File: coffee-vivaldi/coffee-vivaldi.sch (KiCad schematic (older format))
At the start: 74 parts, among them J1 Conn_Coaxial, J2 AudioPlug3, SW1 SW_SPDT, U1 Opamp_Quad_Generic, U3 OPA1604

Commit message: Added chosen RF components to library and schematic
VCO, PA, and the mixer.
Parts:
- removed C?: 1000p, symbol Device:C
- removed C? (x2): 1.5p, symbol Device:C
- removed C? (x5): 0.1u, symbol Device:C
- removed C? (x3): 47p, symbol Device:C
- removed C?: 10u, symbol Device:C
- removed L?: 10n, symbol Device:L
- removed R?: 10, symbol Device:R
- removed R?: 619, symbol Device:R
- removed R?: 100k, symbol Device:R
- removed R?: T2, symbol Device:R
- removed R?: T1, symbol Device:R
- removed U?: MAAPSS0075, symbol HS2_Parts:MAAPSS0075
- added C?: 0.1uF, symbol Device:C
- added C? (x2): 220pF, symbol Device:C
- added C? (x4): 100uF, symbol Device:C
- added C?: CP, symbol Device:CP
- added L?: L, symbol Device:L
- added R? (x4): 7.15K, symbol Device:R
- added U?: MAX2750AUA+, symbol coffee-vivaldi-rescue:MAX2750AUA+-coffee-vivaldi-cache
- added U?: SE2565T-R, symbol coffee-vivaldi-rescue:SE2565T-R-coffee-vivaldi-cache
- added U?: MAX2681EUT+T, symbol coffee-vivaldi-rescue:MAX2681EUT+T-coffee-vivaldi-cache
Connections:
- net labels added: IF_OUTPUT, INPUT_FROM_SYNTHESIZER, NEEDS_TO_BE_HIGH_TO_TURN_ON_DEVICE, RF_INPUT_MIXER, SHUTDOWN_CONTROL1, TO_ATTENUATOR, TO_VCC, VCC_MIXER
- net labels removed: RFIN, RFOUT, VCC, Ven, Vm
- wire segments 180 -> 196
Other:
- note added: "MIXER"
- note added: "PA"
- note added: "VCO"
- moved on the sheet: BT1, BT2, C1, C10, C11, C12, C13, C2, C3, C4, C5, C6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

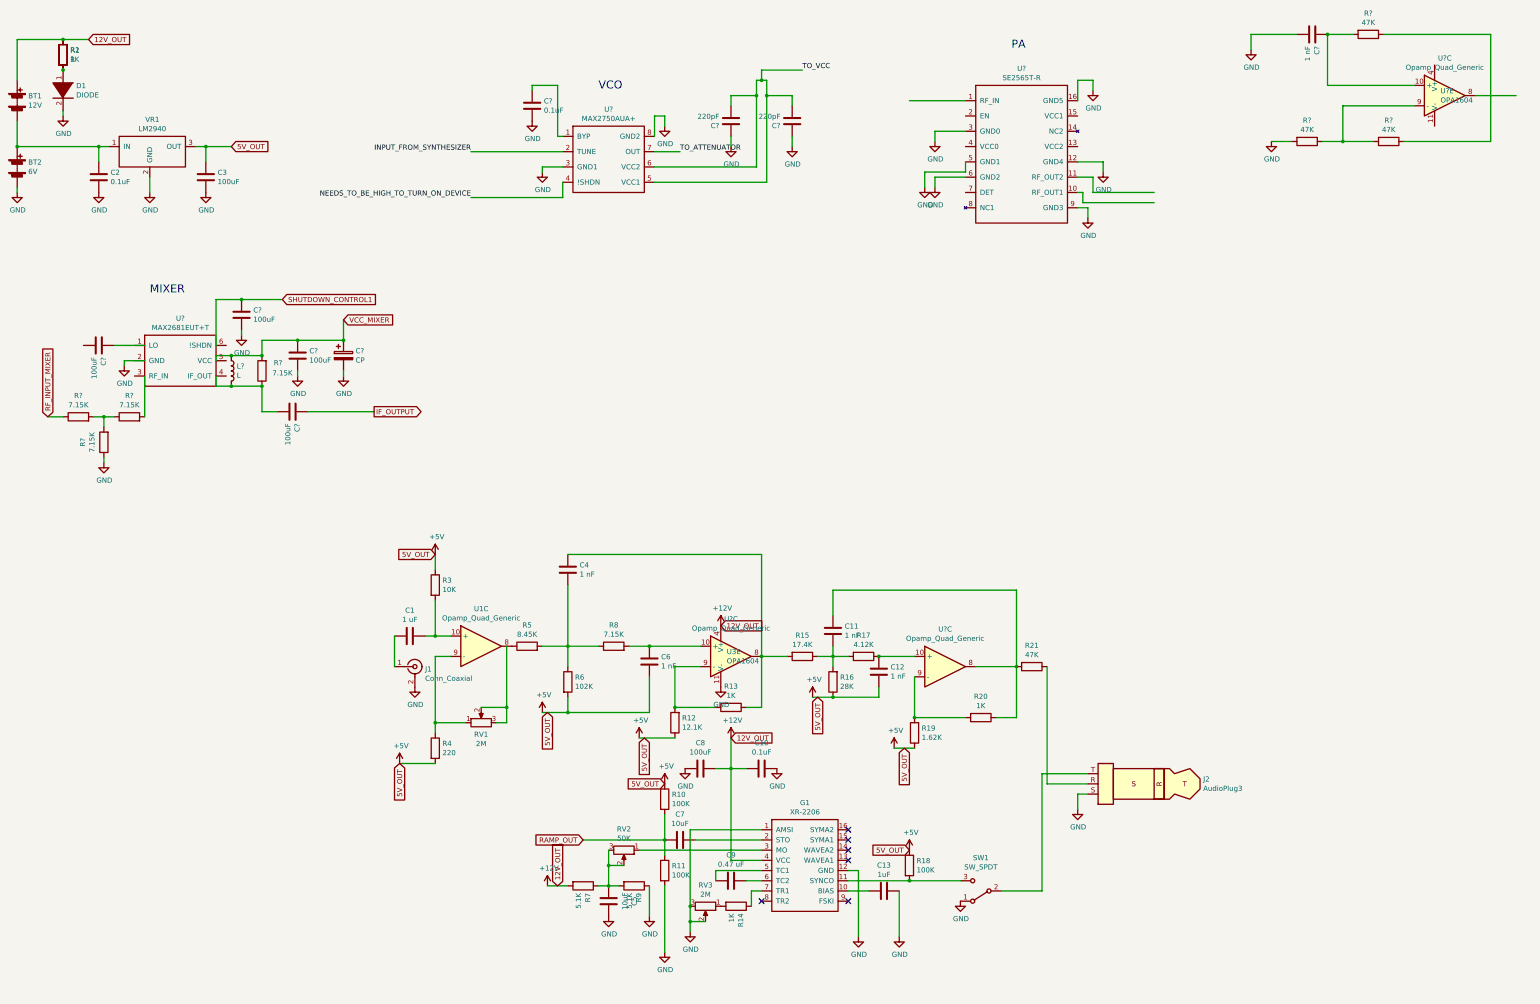
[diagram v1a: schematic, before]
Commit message: Adding passive elements with the RF chips
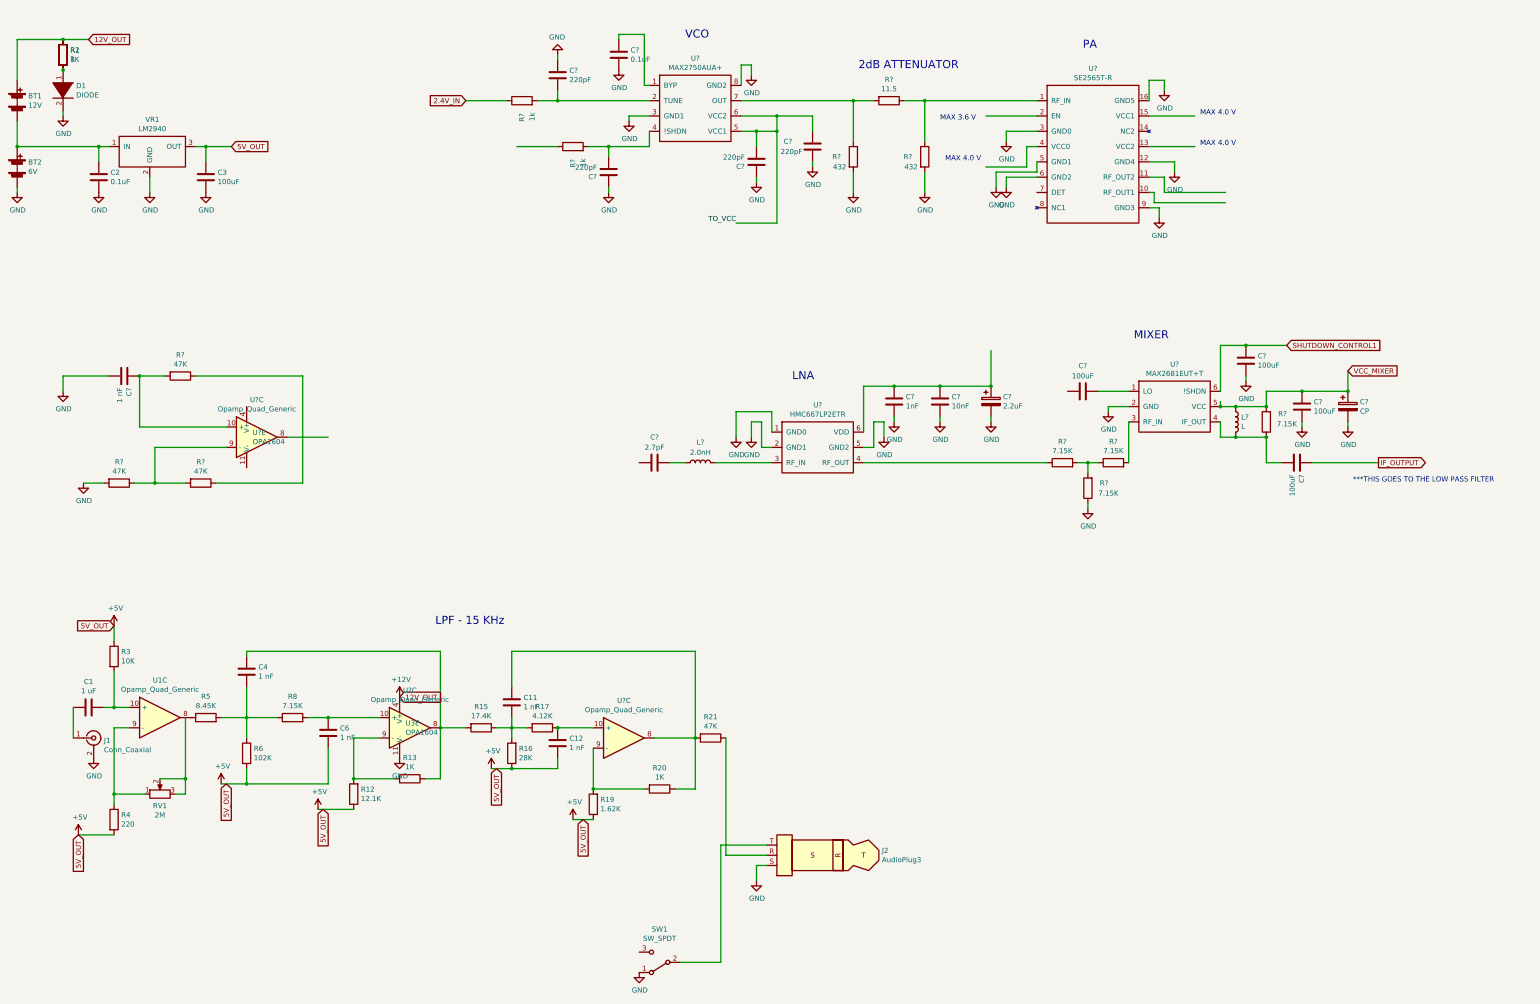
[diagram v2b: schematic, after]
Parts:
- removed C10: 0.1uF, symbol Device:C
- removed C13: 1uF, symbol Device:C
- removed C5, C7: 10uF, symbol Device:C
- removed C8: 100uF, symbol Device:C
- removed C9: 0.47 uF, symbol Device:C
- removed G1: XR-2206, symbol HS2_Parts:XR-2206
- removed R10, R11, R18: 100K, symbol Device:R
- removed R14: 1K, symbol Device:R
- removed R7, R9: 5.1K, symbol Device:R
- removed RV2: 50K, symbol Device:R_POT
- removed RV3: 2M, symbol Device:R_POT
- removed U?: MAX2681EUT+T, symbol coffee-vivaldi-rescue:MAX2681EUT+T-coffee-vivaldi-cache
- added C?: 2.7pF, symbol Device:C
- added C?: 1nF, symbol Device:C
- added C?: 2.2uF, symbol Device:CP
- added C?: 10nF, symbol Device:C
- added C? (x2): 220pF, symbol Device:C
- added L?: 2.0nH, symbol Device:L
- added R? (x2): 1k, symbol Device:R
- added R?: 11.5, symbol Device:R
- added R? (x2): 432, symbol Device:R
- added U?: HMC667LP2ETR, symbol coffee-vivaldi-rescue:HMC667LP2ETR-coffee-vivaldi-cache
- added U?: MAX2681EUT+T, symbol coffee-vivaldi-rescue:MAX2681EUT+T-coffee-vivaldi-cache
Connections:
- net labels added: 2.4V_IN
- net labels removed: INPUT_FROM_SYNTHESIZER, NEEDS_TO_BE_HIGH_TO_TURN_ON_DEVICE, RAMP_OUT, RF_INPUT_MIXER, TO_ATTENUATOR
- wire segments 196 -> 199
- no-connect marks 6 -> 0
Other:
- note added: "***THIS GOES TO THE LOW PASS FILTER"
- note added: "2dB ATTENUATOR"
- note added: "LNA"
- note added: "LPF - 15 KHz"
- note added: "MAX 3.6 V"
- note added: "MAX 4.0 V"
- moved on the sheet: C1, C11, C12, C4, C6, C?, J1, J2, L?, R12, R13, R15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

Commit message: Edited radar schematic
Still a work in progress.
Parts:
- removed J1: Conn_Coaxial, symbol Connector:Conn_Coaxial
- removed R? (x4): 7.15K, symbol Device:R
- removed U?: HMC667LP2ETR, symbol coffee-vivaldi-rescue:HMC667LP2ETR-coffee-vivaldi-cache
- removed U?: Opamp_Quad_Generic, symbol Device:Opamp_Quad_Generic
- removed U?: MAX2681EUT+T, symbol coffee-vivaldi-rescue:MAX2681EUT+T-coffee-vivaldi-cache
- removed U?: MAX2750AUA+, symbol coffee-vivaldi-rescue:MAX2750AUA+-coffee-vivaldi-cache
- removed U?: SE2565T-R, symbol coffee-vivaldi-rescue:SE2565T-R-coffee-vivaldi-cache
- added C10: 0.1uF, symbol Device:C
- added C13: 1uF, symbol Device:C
- added C5, C7: 10uF, symbol Device:C
- added C8: 100uF, symbol Device:C
- added C9: 0.47 uF, symbol Device:C
- added C?: 270pF, symbol Device:C
- added G1: XR-2206, symbol HS2_Parts:XR-2206
- added L?: 1.2nH, symbol Device:L
- added R10, R11, R18: 100K, symbol Device:R
- added R14: 1K, symbol Device:R
- added R7, R9: 5.1K, symbol Device:R
- added RV2: 50K, symbol Device:R_POT
- added RV3: 2M, symbol Device:R_POT
- added U?: MAX2681EUT+T, symbol HS2_Parts:MAX2681EUT+T
- added U?: HMC667LP2ETR, symbol HS2_Parts:HMC667LP2ETR
- added U?: MAX2750AUA+, symbol HS2_Parts:MAX2750AUA+
- added U?: SE2565T-R, symbol HS2_Parts:SE2565T-R
- added U? (x2): SMA_PCB_Edge_Mount, symbol HS2_Parts:SMA_PCB_Edge_Mount
- added U?: Opamp_Quad_Generic, symbol Device:Opamp_Quad_Generic
- C?: value 100uF -> 3pF
- C?: value CP -> 10uF
- L?: value L -> 82nH
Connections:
- net labels added: 3.6V_IN, 3.6V_OUT, 4.0V_IN, 4.0V_OUT, COUPLER_SIGNAL, IF_SIGNAL, RAMP_SIGNAL
- net labels removed: 2.4V_IN, IF_OUTPUT, SHUTDOWN_CONTROL1, TO_VCC
- wire segments 199 -> 243
- no-connect marks 0 -> 7
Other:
- note added: "MODULATOR"
- note added: "Rx"
- note added: "Tx"
- note removed: "***THIS GOES TO THE LOW PASS FILTER"
- note removed: "MAX 3.6 V"
- note removed: "MAX 4.0 V"
- moved on the sheet: C1, C6, C?, L?, R21, R3, R4, R6, R8, R?, SW1, U1C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

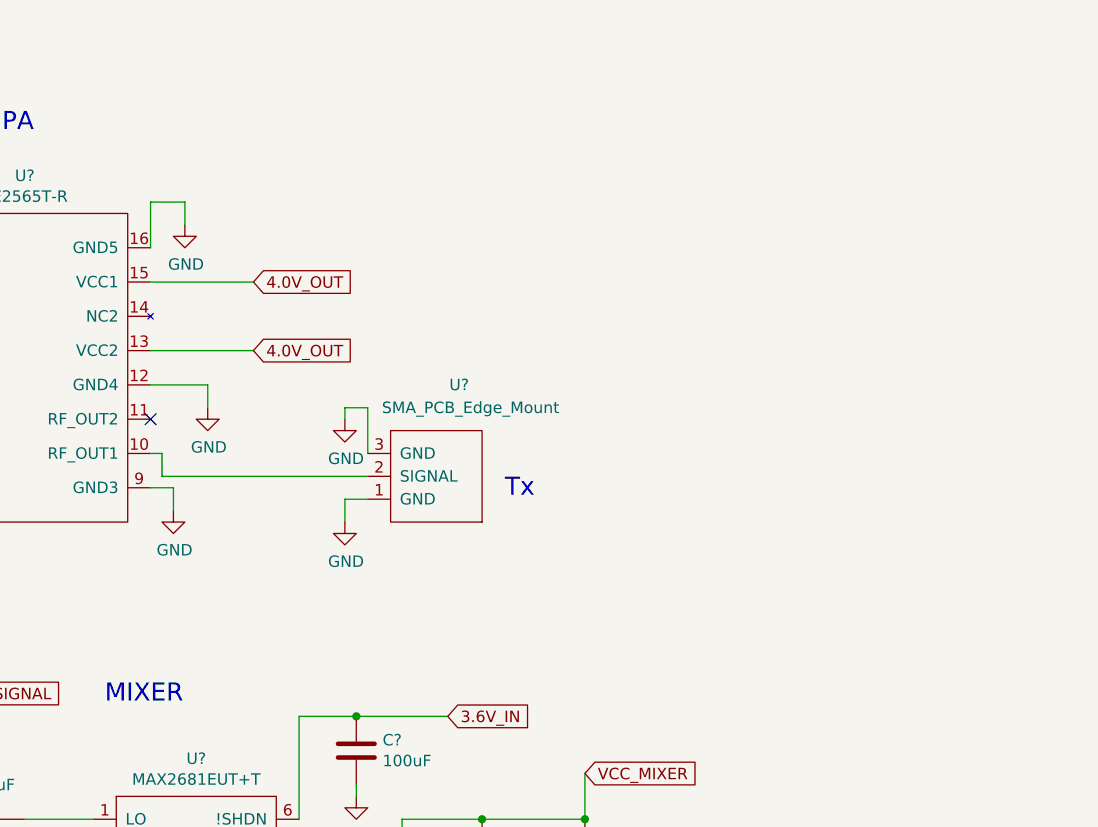
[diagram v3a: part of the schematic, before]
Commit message: Added directional coupler, added impedence control
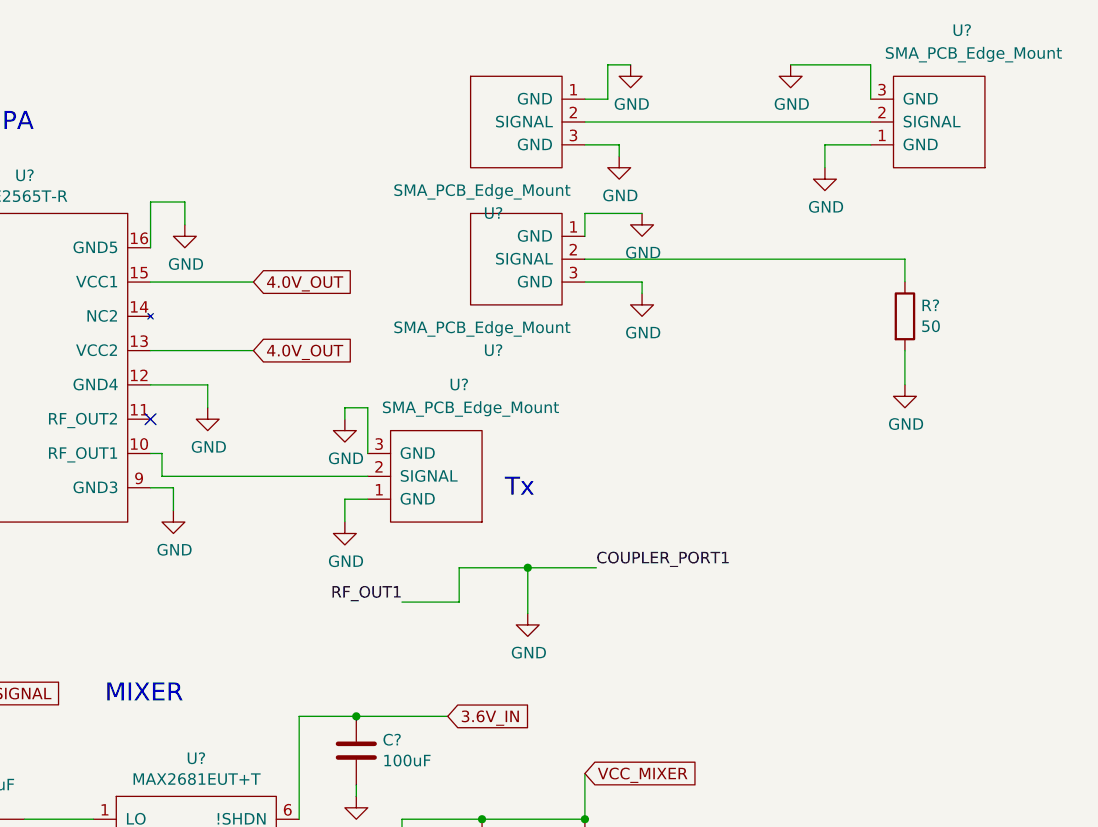
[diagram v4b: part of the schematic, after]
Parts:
- added R?: 50, symbol Device:R
- added U? (x3): SMA_PCB_Edge_Mount, symbol HS2_Parts:SMA_PCB_Edge_Mount
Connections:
- net GND: now also R?.2, U?.1 (GND), U?.1 (GND), U?.1 (GND), U?.3 (GND), U?.3 (GND), U?.3 (GND)
- new net: U?.2 (SIGNAL), U?.2 (SIGNAL)
- new net: R?.1, U?.2 (SIGNAL)
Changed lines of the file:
@@
 Text GLabel 5900 2300 0    50   Input ~ 0
 3.6V_OUT
-Wire Wire Line
-	13050 2850 12150 2850
 Text Notes 13650 2950 0    79   ~ 0
 Tx
@@
 Text GLabel 8050 3050 0    50   Input ~ 0
 5V_OUT
+$Comp
+L HS2_Parts:SMA_PCB_Edge_Mount U?
+U 1 1 60438739
+P 13700 1500
+F 0 "U?" H 13600 1300 50  0000 C CNN
+F 1 "SMA_PCB_Edge_Mount" H 13550 1400 50  0000 C CNN
+F 2 "" H 13700 1500 50  0001 C CNN
+F 3 "" H 13700 1500 50  0001 C CNN
+	1    13700 1500
+	1    0    0    -1
+$EndComp
+$Comp
+L HS2_Parts:SMA_PCB_Edge_Mount U?
+U 1 1 6043955D
+P 15550 1100
+F 0 "U?" H 15450 900 50  0000 C CNN
+F 1 "SMA_PCB_Edge_Mount" H 15400 1000 50  0000 C CNN
+F 2 "" H 15550 1100 50  0001 C CNN
+F 3 "" H 15550 1100 50  0001 C CNN
+	1    15550 1100
+	-1   0    0    1
+$EndComp
+Wire Wire Line
+	12150 2850 13050 2850
+Wire Wire Line
+	13200 3400 13450 3400
+Wire Wire Line
+	13450 3400 13450 3250
+Wire Wire Line
+	13450 3250 13750 3250
+Wire Wire Line
+	14000 1300 15250 1300
+$Comp
+L HS2_Parts:SMA_PCB_Edge_Mount U?
+U 1 1 604AA8E4
+P 13700 2100
+F 0 "U?" H 13600 1900 50  0000 C CNN
+F 1 "SMA_PCB_Edge_Mount" H 13550 2000 50  0000 C CNN
+F 2 "" H 13700 2100 50  0001 C CNN
+F 3 "" H 13700 2100 50  0001 C CNN
+	1    13700 2100
+	1    0    0    -1
+$EndComp
+$Comp
+L power:GND #PWR?
+U 1 1 604BD349
+P 14250 1700
+F 0 "#PWR?" H 14250 1450 50  0001 C CNN
+F 1 "GND" H 14255 1527 50  0000 C CNN
+F 2 "" H 14250 1700 50  0001 C CNN
+F 3 "" H 14250 1700 50  0001 C CNN
+	1    14250 1700
+	1    0    0    -1
+$EndComp
+$Comp
+L power:GND #PWR?
+U 1 1 604BD6D7
+P 14250 2050
+F 0 "#PWR?" H 14250 1800 50  0001 C CNN
+F 1 "GND" H 14255 1877 50  0000 C CNN
+F 2 "" H 14250 2050 50  0001 C CNN
+F 3 "" H 14250 2050 50  0001 C CNN
+	1    14250 2050
+	1    0    0    -1
+$EndComp
+$Comp
+L power:GND #PWR?
+U 1 1 604BDAC7
+P 15400 2450
+F 0 "#PWR?" H 15400 2200 50  0001 C CNN
+F 1 "GND" H 15405 2277 50  0000 C CNN
+F 2 "" H 15400 2450 50  0001 C CNN
+F 3 "" H 15400 2450 50  0001 C CNN
+	1    15400 2450
+	1    0    0    -1
+$EndComp
+Wire Wire Line
+	14250 1700 14000 1700
+Wire Wire Line
+	14000 1700 14000 1800
+Wire Wire Line
+	14000 2000 14250 2000
+Wire Wire Line
+	14250 2000 14250 2050
+$Comp
+L power:GND #PWR?
+U 1 1 605037D3
+P 14150 1450
+F 0 "#PWR?" H 14150 1200 50  0001 C CNN
+F 1 "GND" H 14155 1277 50  0000 C CNN
+F 2 "" H 14150 1450 50  0001 C CNN
+F 3 "" H 14150 1450 50  0001 C CNN
+	1    14150 1450
+	1    0    0    -1
+$EndComp
+Wire Wire Line
+	14000 1400 14150 1400
+Wire Wire Line
+	14150 1400 14150 1450
+$Comp
+L power:GND #PWR?
+U 1 1 6051563D
+P 14200 1050
+F 0 "#PWR?" H 14200 800 50  0001 C CNN
+F 1 "GND" H 14205 877 50  0000 C CNN
+F 2 "" H 14200 1050 50  0001 C CNN
+F 3 "" H 14200 1050 50  0001 C CNN
+	1    14200 1050
+	1    0    0    -1
+$EndComp
+Wire Wire Line
+	14000 1200 14100 1200
+Wire Wire Line
+	14100 1200 14100 1050
+Wire Wire Line
+	14100 1050 14200 1050
+$Comp
+L power:GND #PWR?
+U 1 1 60527B36
+P 14900 1050
+F 0 "#PWR?" H 14900 800 50  0001 C CNN
+F 1 "GND" H 14905 877 50  0000 C CNN
+F 2 "" H 14900 1050 50  0001 C CNN
+F 3 "" H 14900 1050 50  0001 C CNN
+	1    14900 1050
+	1    0    0    -1
+$EndComp
+Wire Wire Line
+	14900 1050 15250 1050
+Wire Wire Line
+	15250 1050 15250 1200
+$Comp
+L power:GND #PWR?
+U 1 1 6053A413
+P 15050 1500
+F 0 "#PWR?" H 15050 1250 50  0001 C CNN
+F 1 "GND" H 15055 1327 50  0000 C CNN
+F 2 "" H 15050 1500 50  0001 C CNN
+F 3 "" H 15050 1500 50  0001 C CNN
+	1    15050 1500
+	1    0    0    -1
+$EndComp
+Wire Wire Line
+	15050 1500 15050 1400
+Wire Wire Line
+	15050 1400 15250 1400
+$Comp
+L power:GND #PWR?
+U 1 1 6054DD37
+P 13750 3450
+F 0 "#PWR?" H 13750 3200 50  0001 C CNN
+F 1 "GND" H 13755 3277 50  0000 C CNN
+F 2 "" H 13750 3450 50  0001 C CNN
+F 3 "" H 13750 3450 50  0001 C CNN
+	1    13750 3450
+	1    0    0    -1
+$EndComp
+Wire Wire Line
+	13750 3250 13750 3450
+$Comp
+L Device:R R?
+U 1 1 6058F77C
+P 15400 2150
+F 0 "R?" H 15470 2196 50  0000 L CNN
+F 1 "50" H 15470 2105 50  0000 L CNN
+F 2 "" V 15330 2150 50  0001 C CNN
+F 3 "~" H 15400 2150 50  0001 C CNN
+	1    15400 2150
+	1    0    0    -1
+$EndComp
+Wire Wire Line
+	15400 2300 15400 2450
+Wire Wire Line
+	15400 1900 15400 2000
+Wire Wire Line
+	14000 1900 15400 1900
+Wire Wire Line
+	13750 3250 14050 3250
+Connection ~ 13750 3250
+Text Label 13200 3400 2    50   ~ 0
+RF_OUT1
+Text Label 14050 3250 0    50   ~ 0
+COUPLER_PORT1
 $EndSCHEMATC
